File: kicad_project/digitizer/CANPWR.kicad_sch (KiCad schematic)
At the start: 18 parts, among them IC201 MAX3059ASA+T UPSTREAM, IC202 MAX6035AAUR50+T, IC203 MAX3059ASA+T DOWNSTREAM, IC204 MAX6043BAUT33+T, J201 DT15-4P (UPSTREAM), J202 DT06-4S (DOWNSTREAM)

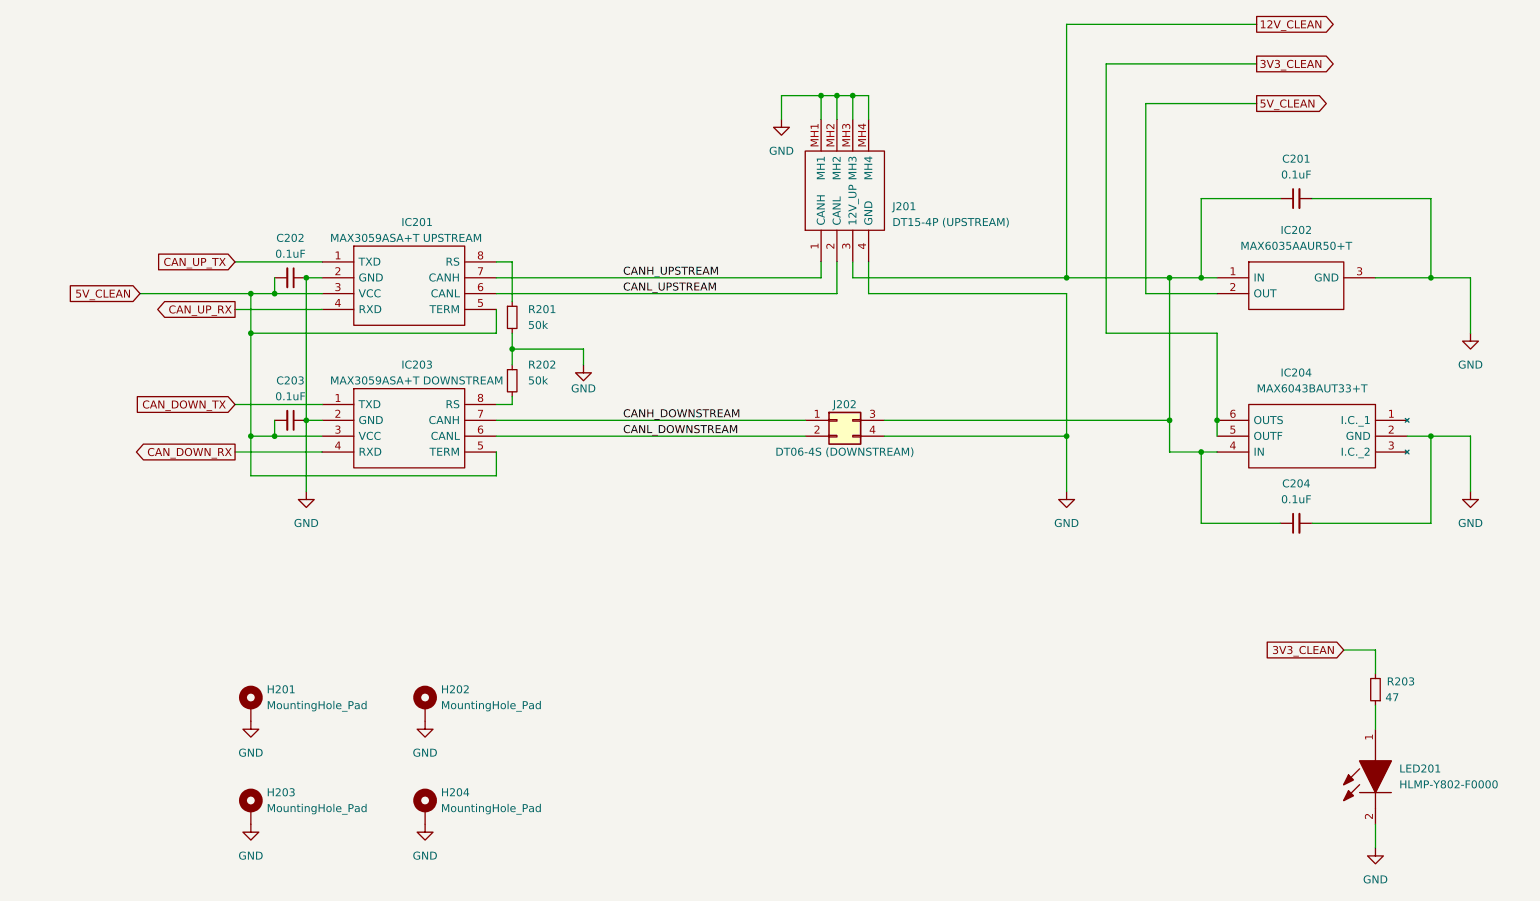
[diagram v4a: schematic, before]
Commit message: added some 0R resistors to pads to allow for easier board modding
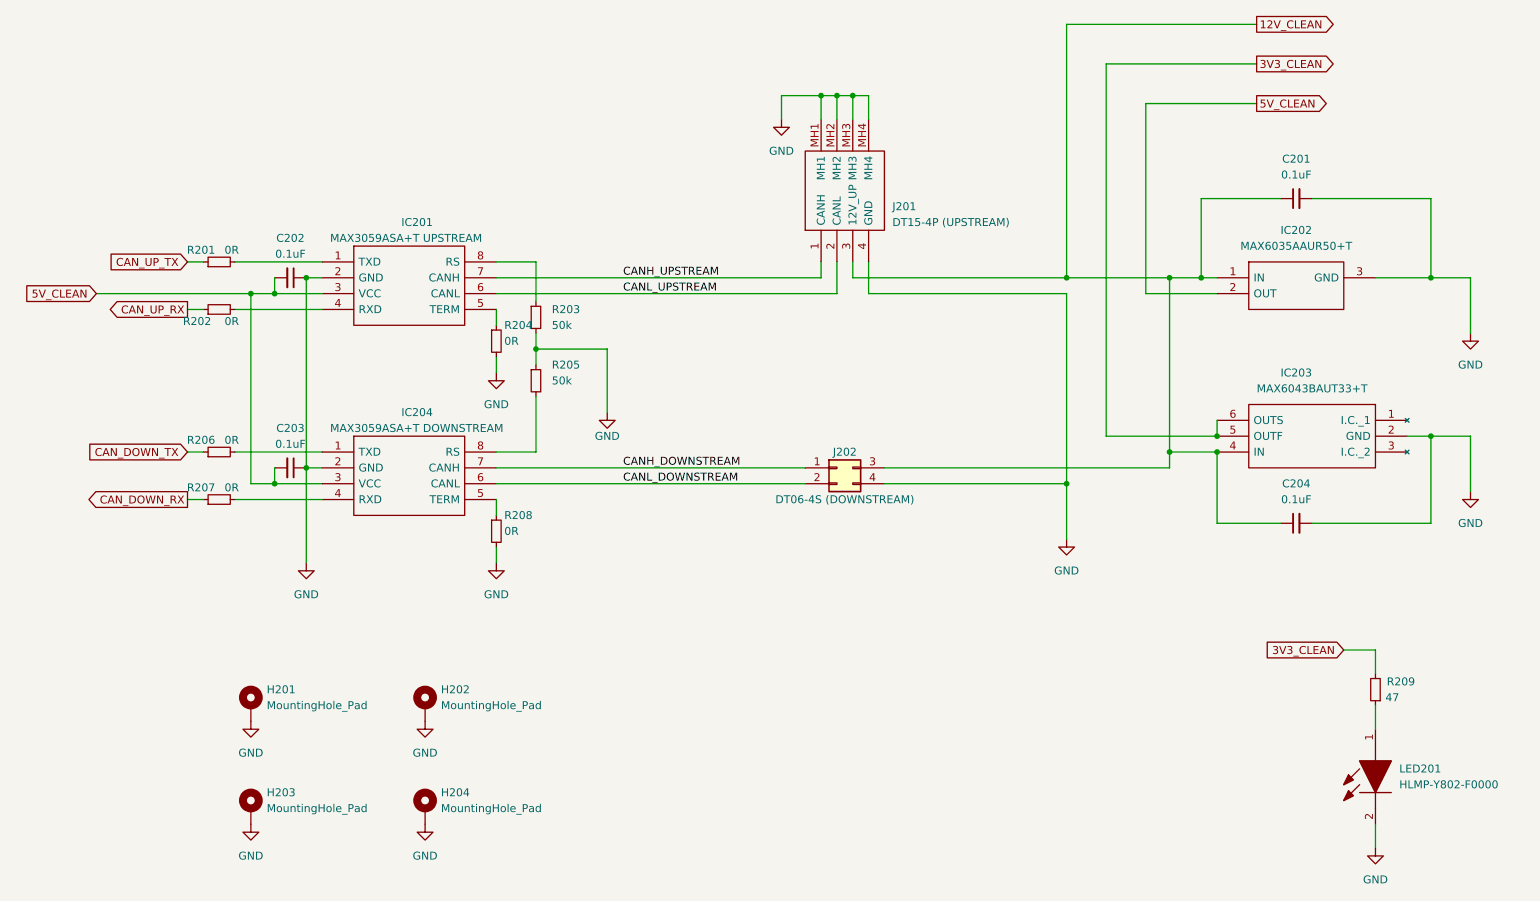
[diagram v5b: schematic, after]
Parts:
- added R201, R202, R204, R206, R207, R208: 0R, Resistor_SMD:R_0805_2012Metric_Pad1.20x1.40mm_HandSolder, symbol Device:R_Small
- renumbered IC204 to IC203, IC203 to IC204, R201 to R203, R202 to R205, R203 to R209
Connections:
- net 5V_CLEAN: no longer IC201.5 (TERM), IC204.5 (TERM)
- net CAN_DOWN_RX: now also R207.1; no longer IC204.4 (RXD)
- net CAN_DOWN_TX: now also R206.1; no longer IC204.1 (TXD)
- net CAN_UP_RX: now also R202.1; no longer IC201.4 (RXD)
- net CAN_UP_TX: now also R201.1; no longer IC201.1 (TXD)
- net GND: now also R204.2, R208.2
- new net: IC201.4 (RXD), R202.2
- new net: IC201.5 (TERM), R204.1
- new net: IC201.1 (TXD), R201.2
- new net: IC204.4 (RXD), R207.2
- new net: IC204.1 (TXD), R206.2
- new net: IC204.5 (TERM), R208.1
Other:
- moved on the sheet: C203, IC204, J202, R203, R205

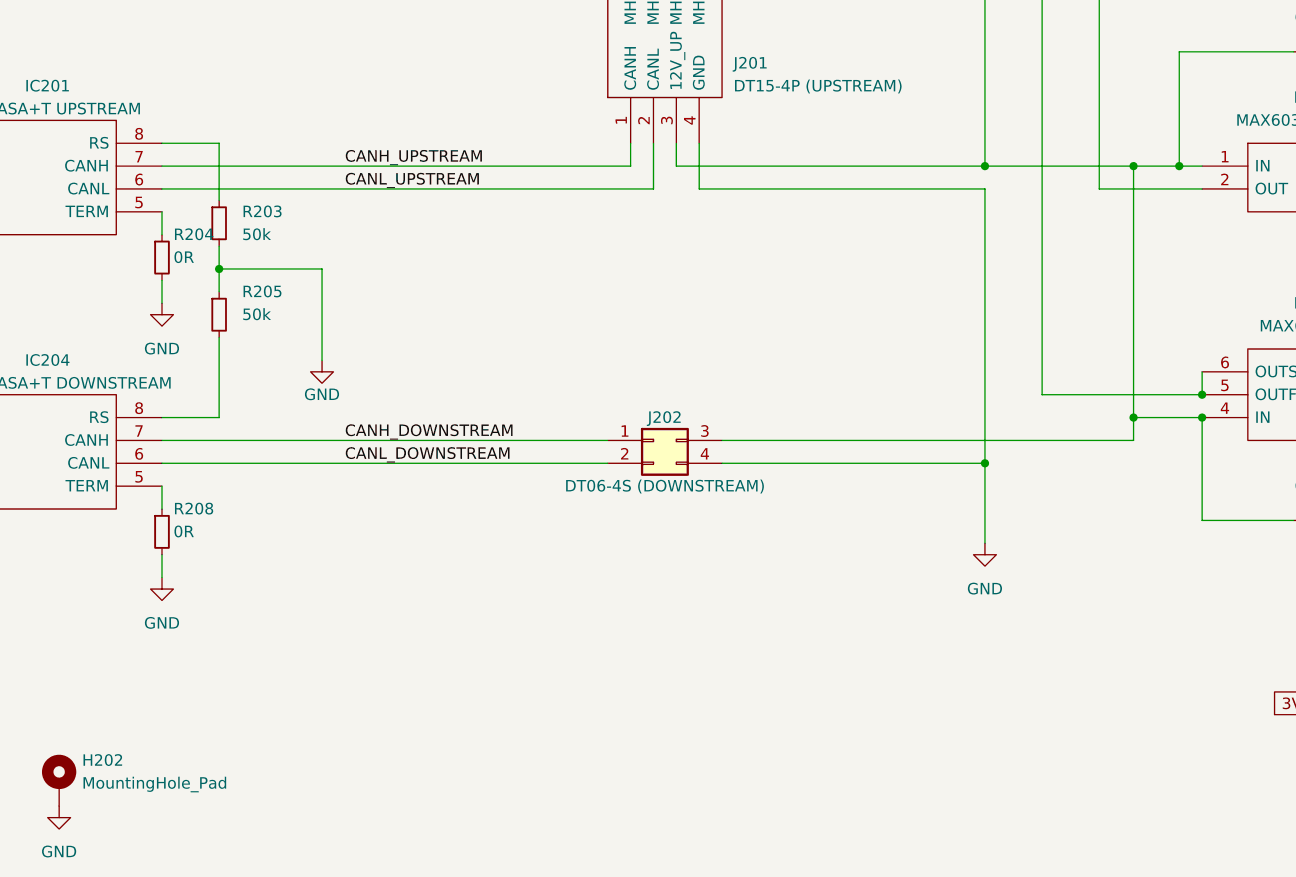
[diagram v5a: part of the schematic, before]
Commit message: added TVS diodes to upstream and downstream connector signals
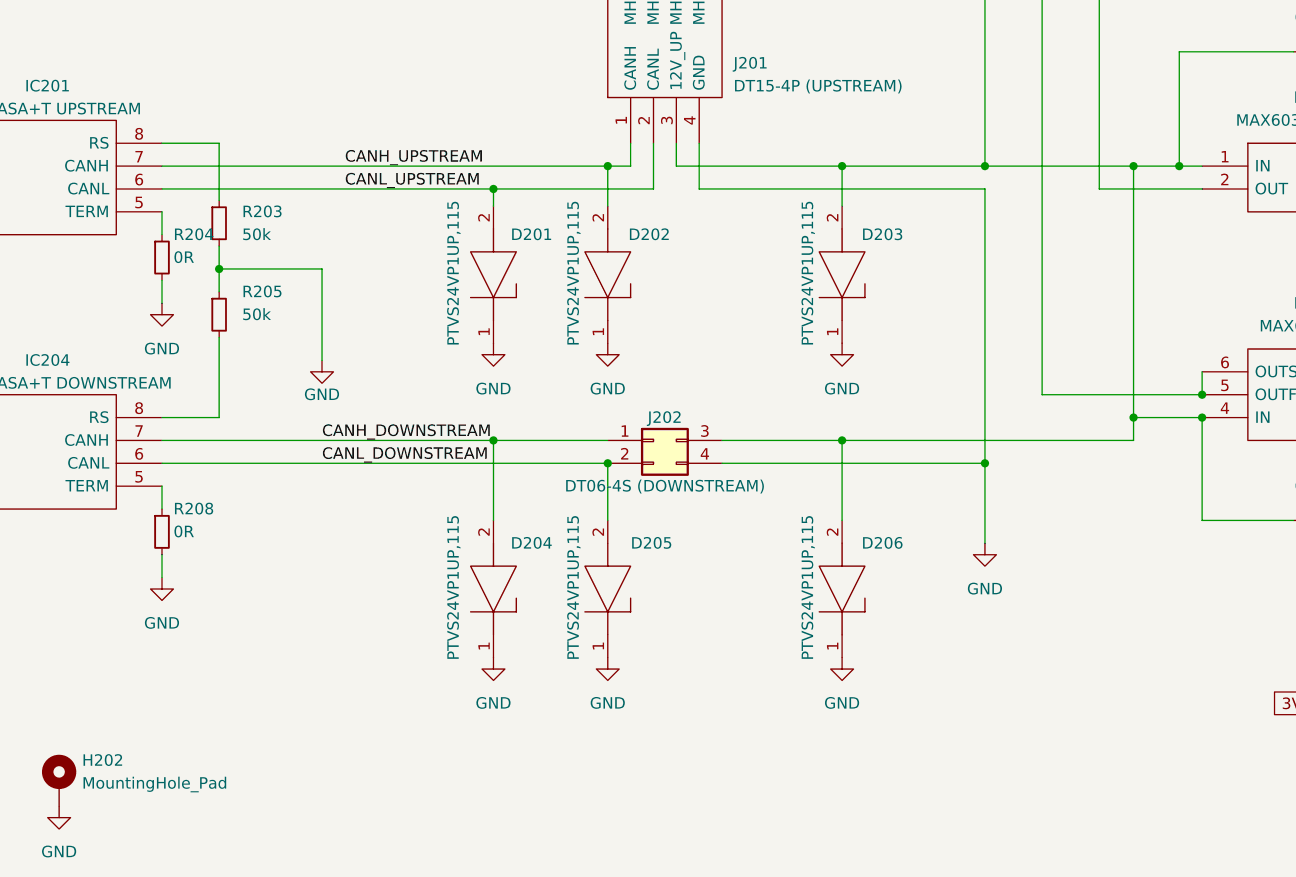
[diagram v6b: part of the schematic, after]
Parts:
- added D201, D202, D203, D204, D205, D206: PTVS24VP1UP,115, PMEG3050EP115, symbol SamacSys_Parts:PTVS24VP1UP,115
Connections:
- net 12V_CLEAN: now also D203.2, D206.2
- net CANH_DOWNSTREAM: now also D204.2
- net CANH_UPSTREAM: now also D202.2
- net CANL_DOWNSTREAM: now also D205.2
- net CANL_UPSTREAM: now also D201.2
- net GND: now also D201.1, D202.1, D203.1, D204.1, D205.1, D206.1

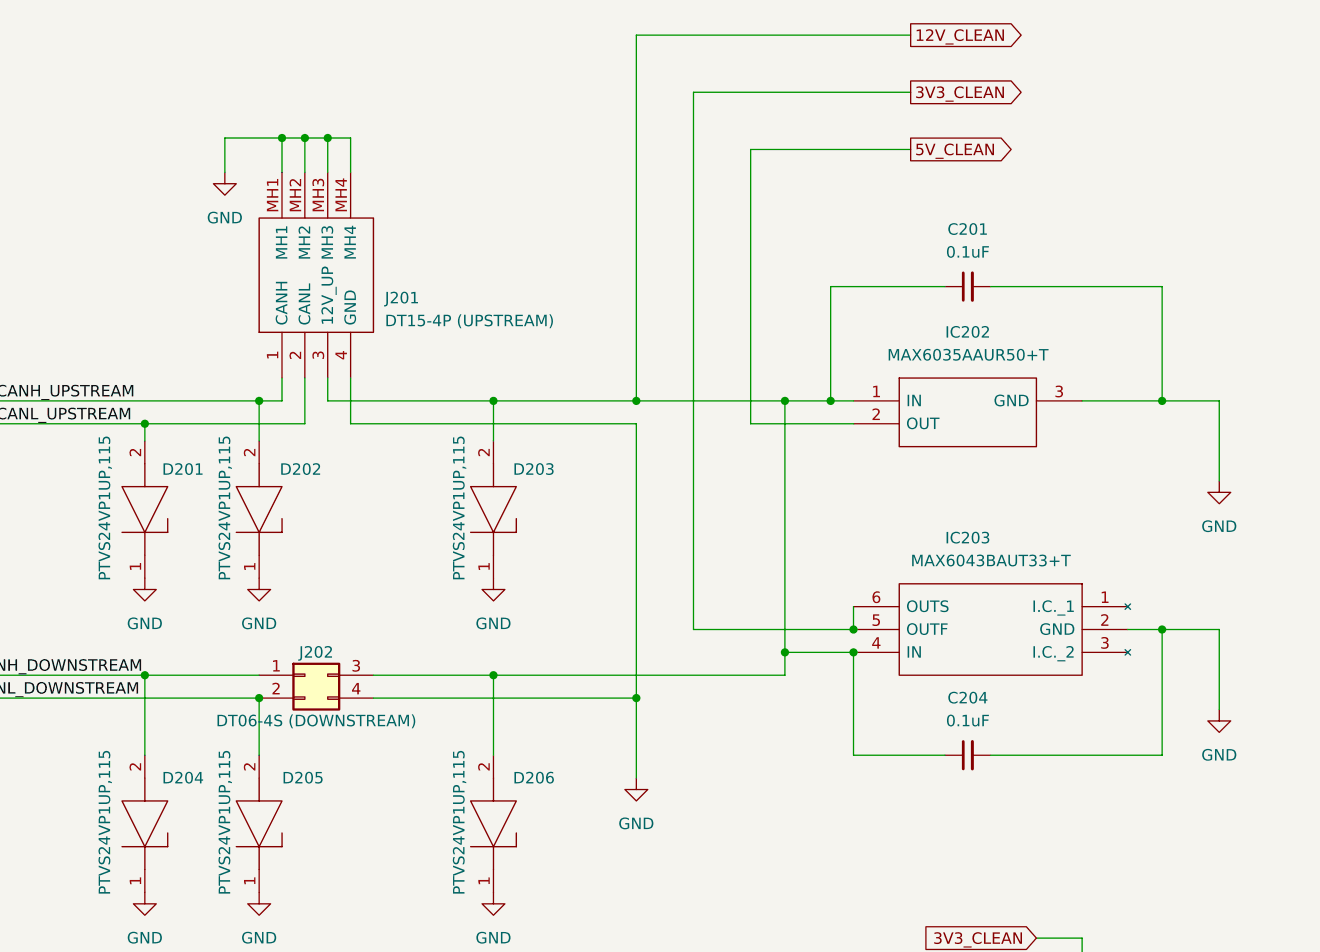
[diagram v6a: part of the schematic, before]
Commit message: added TVS diodes to 3V3 and 5V rails as well
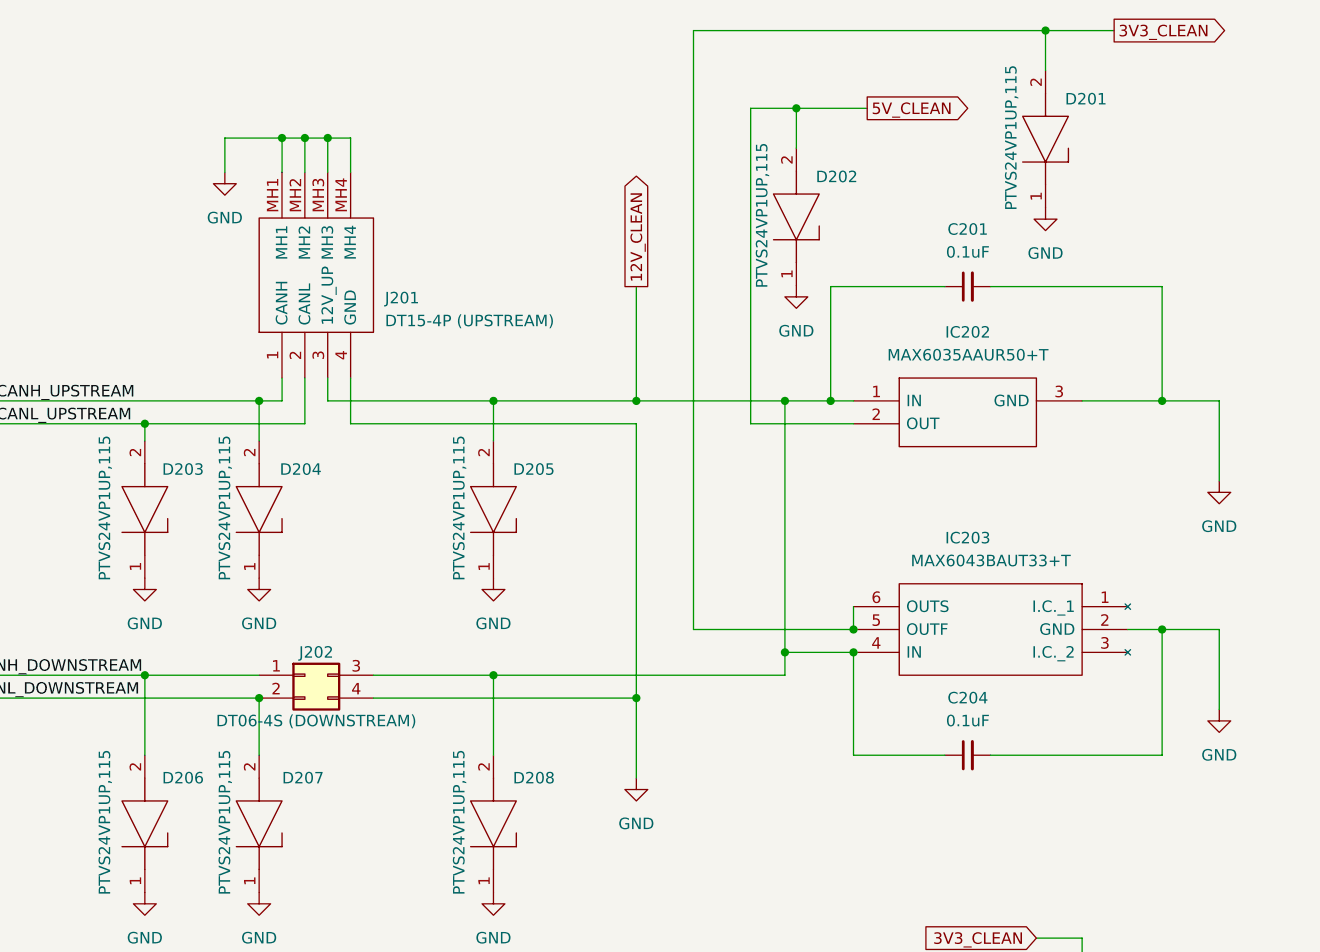
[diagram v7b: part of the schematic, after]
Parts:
- added D201, D202: PTVS24VP1UP,115, PMEG3050EP115, symbol SamacSys_Parts:PTVS24VP1UP,115
- renumbered D201 to D203, D202 to D204, D203 to D205, D204 to D206, D205 to D207, D206 to D208
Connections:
- net 3V3_CLEAN: now also D201.2
- net 5V_CLEAN: now also D202.2
- net GND: now also D201.1, D202.1
